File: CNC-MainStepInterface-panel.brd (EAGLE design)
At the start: 99.1 x 84.1 mm, 30 parts, among them IC10 ATTINY84-20PU, IC11 74HCT595N, IC1A ARDUINO_MINI, IC1B ATMEGA328P_PDIP, IC2 74HCT541N, IC3 74HCT541N, IC4 74HCT541N, IC5 74HCT541N, IC6 ATTINY2313A-PU, IC7 74HCT125N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

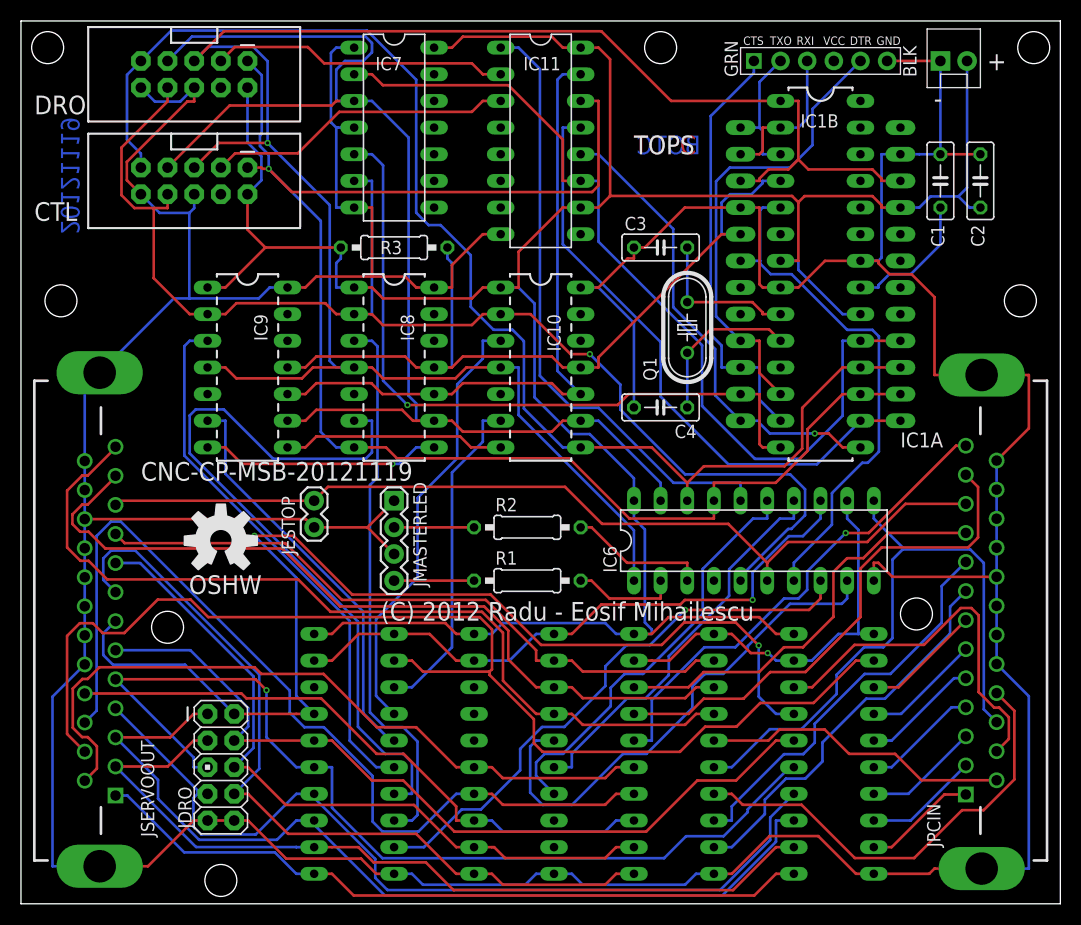
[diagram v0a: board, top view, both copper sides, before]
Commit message: Minor cosmetic changes, following production run. - added 45 degree bends to all 90 corners - straightened up two traces
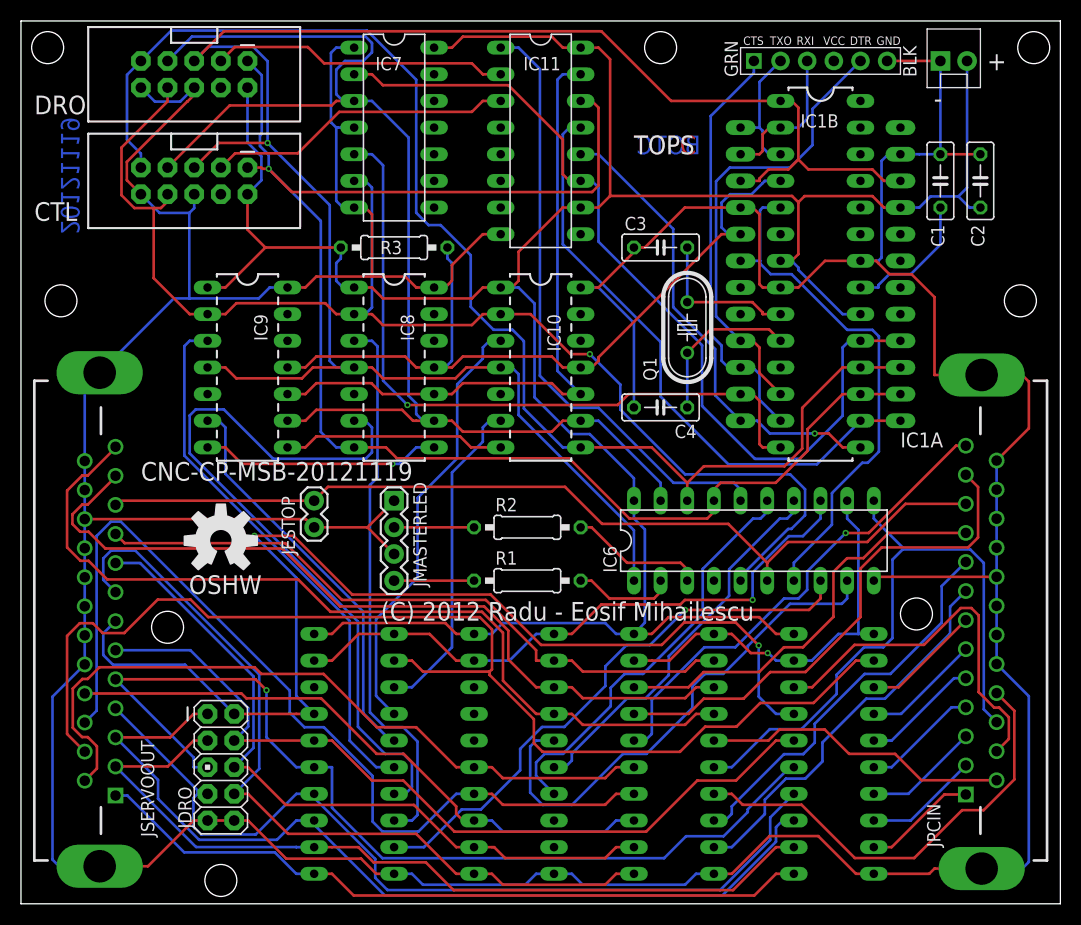
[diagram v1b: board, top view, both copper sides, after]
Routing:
- net GND: track 473.0 -> 467.0 mm
- net VCC: track 258.5 -> 255.6 mm
- net !INT0: track 75.5 -> 74.2 mm
- net SCK_INT: track 85.2 -> 84.1 mm
- net CLK: track 126.0 -> 124.9 mm
- net MOSI: track 149.6 -> 148.5 mm
- net !RESET: track 190.2 -> 189.3 mm
- net X_STEP: track 72.1 -> 71.3 mm
- net SCK: track 127.8 -> 127.1 mm
- net !CTS: track 40.9 -> 40.1 mm
- net WDT_PWM: track 37.7 -> 36.9 mm

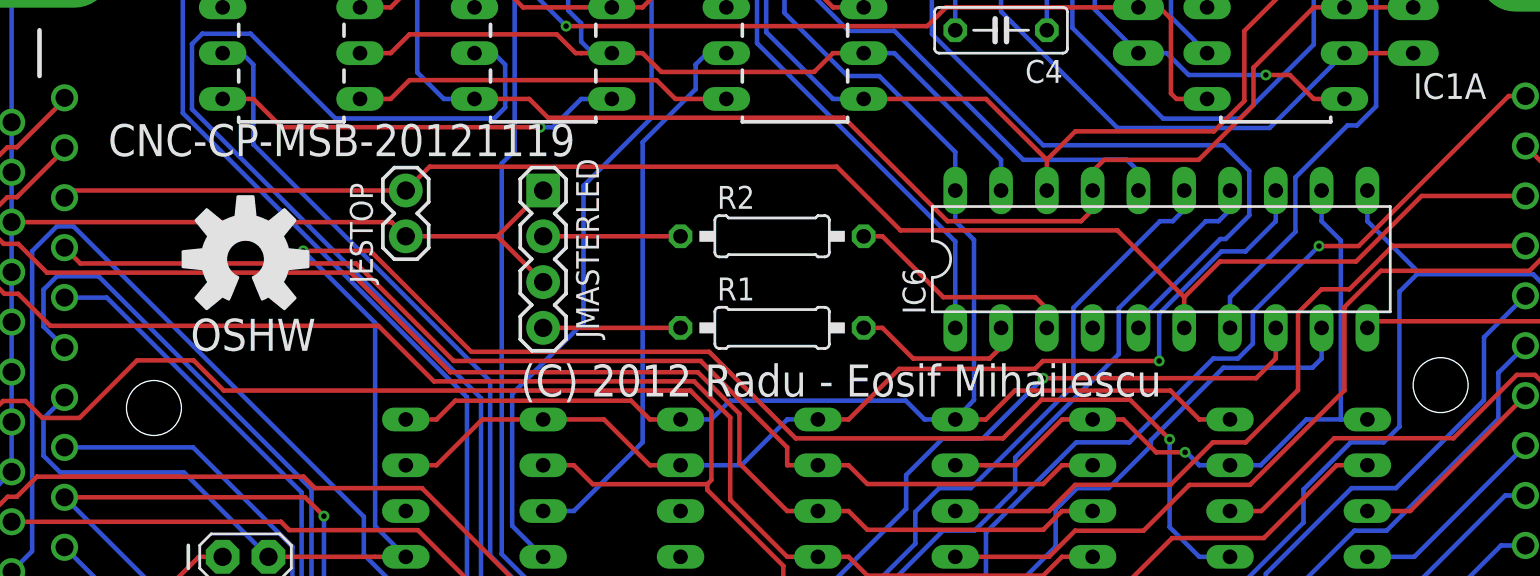
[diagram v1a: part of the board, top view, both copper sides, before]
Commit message: BUGFIX: [XYZ]_LIMIT# not connected to [XYZ]_HOME# - when panelizing Main + Stepper + Interface on the same board, I forgot to make LIMIT the same as HOME. This will have to be reworked by hand during assembly. - only added net connections, PCB artwork to be updated at the next autorouter run - added 45 degree corners to some traces that escaped the first pass
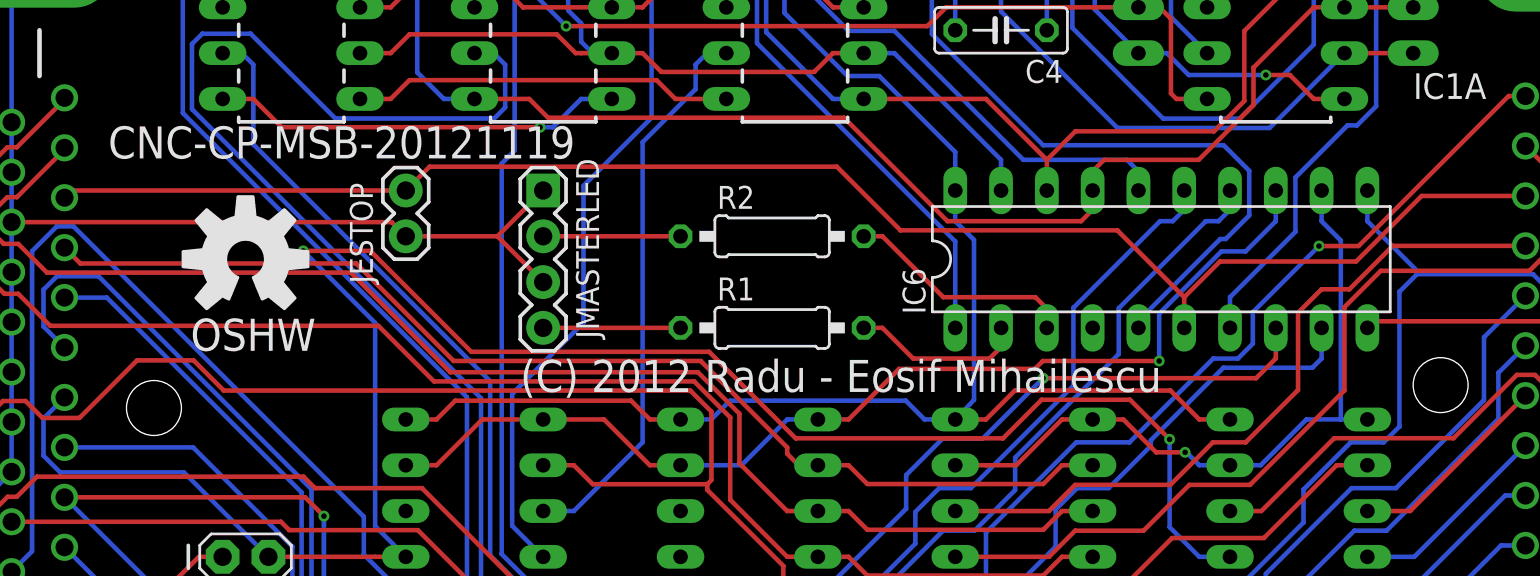
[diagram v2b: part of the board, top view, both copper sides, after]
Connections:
- removed net !X_LIMIT: IC8.5
- removed net !Y_LIMIT: IC9.5
- removed net !Z_LIMIT: IC10.5
- net !X_HOME: now also IC8.5
- net !Y_HOME: now also IC9.5
- net !Z_HOME: now also IC10.5
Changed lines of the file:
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@@
 <text x="58.42" y="71.12" size="1.778" layer="21" font="vector" ratio="15">TOPS</text>
 <text x="64.77" y="71.12" size="1.778" layer="22" font="vector" ratio="15" rot="MR0">BOTS</text>
-<text x="11.43" y="40.005" size="1.778" layer="21" font="vector" ratio="15">CNC-CP-MSB-20121119</text>
+<text x="11.43" y="39.878" size="1.778" layer="21" font="vector" ratio="15">CNC-CP-MSB-20121119</text>
 <text x="3.81" y="63.5" size="1.778" layer="16" font="vector" ratio="15" rot="MR90">20121119</text>
-<text x="34.29" y="26.67" size="1.778" layer="21" font="vector" ratio="15">(C) 2012 Radu - Eosif Mihailescu</text>
+<text x="34.29" y="26.924" size="1.778" layer="21" font="vector" ratio="15">(C) 2012 Radu - Eosif Mihailescu</text>
 <text x="1.27" y="64.77" size="1.778" layer="21" font="vector" ratio="15">CTL</text>
 <text x="1.27" y="74.93" size="1.778" layer="21" font="vector" ratio="15">DRO</text>
@@
 <contactref element="IC5" pad="2"/>
 <contactref element="JSERVOOUT" pad="10"/>
-<wire x1="50.8" y1="22.86" x2="49.0981" y2="22.86" width="0.254" layer="1"/>
+<wire x1="49.0981" y1="23.8468" x2="49.0981" y2="23.495" width="0.254" layer="1"/>
+<wire x1="49.0981" y1="23.495" x2="49.7331" y2="22.86" width="0.254" layer="1"/>
+<wire x1="49.7331" y1="22.86" x2="50.8" y2="22.86" width="0.254" layer="1"/>
 <wire x1="9.01" y1="34.93" x2="9.8868" y2="34.0532" width="0.254" layer="1"/>
 <wire x1="9.8868" y1="34.0532" x2="25.1861" y2="34.0532" width="0.254" layer="1"/>
@@
 <wire x1="30.5946" y1="28.6447" x2="44.3002" y2="28.6447" width="0.254" layer="1"/>
 <wire x1="44.3002" y1="28.6447" x2="49.0981" y2="23.8468" width="0.254" layer="1"/>
-<wire x1="49.0981" y1="23.8468" x2="49.0981" y2="22.86" width="0.254" layer="1"/>
 <wire x1="66.04" y1="22.86" x2="64.3381" y2="22.86" width="0.254" layer="1"/>
 <wire x1="50.8" y1="22.86" x2="52.5019" y2="22.86" width="0.254" layer="1"/>
@@
 <signal name="!X_HOME">
 <contactref element="IC5" pad="16"/>
+<contactref element="IC8" pad="5"/>
+<wire x1="43.18" y1="15.24" x2="31.75" y2="48.26" width="0" layer="19" extent="1-1"/>
 </signal>
 <signal name="!Y_HOME">
 <contactref element="IC5" pad="17"/>
+<contactref element="IC9" pad="5"/>
+<wire x1="43.18" y1="17.78" x2="17.78" y2="48.26" width="0" layer="19" extent="1-1"/>
 </signal>
 <signal name="!Z_HOME">
 <contactref element="IC5" pad="18"/>
+<contactref element="IC10" pad="5"/>
+<wire x1="43.18" y1="20.32" x2="45.72" y2="48.26" width="0" layer="19" extent="1-1"/>
 </signal>
 <signal name="SPINDLE">
@@
 <wire x1="42.9766" y1="75.1585" x2="44.0181" y2="76.2" width="0.254" layer="1"/>
 </signal>
-<signal name="!X_LIMIT">
-<contactref element="IC8" pad="5"/>
-</signal>
-<signal name="!Y_LIMIT">
-<contactref element="IC9" pad="5"/>
-</signal>
-<signal name="!Z_LIMIT">
-<contactref element="IC10" pad="5"/>
-</signal>
 <signal name="MISO_1">
